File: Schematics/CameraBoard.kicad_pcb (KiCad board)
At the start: 2 copper layers, 62.3 x 68 mm, 61 parts, among them J1 Runcam Split 4 v2, J2 USB_C_Receptacle, SW1 SW_Push, SW2 SW_Push, U1 STM32F405RGTx, U2 TPS22917DBVR, U3 TPS22917DBVR, U4 SN65HVD230DR, U5 AMS1117-3.3, U6 TPS22917DBVR

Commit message: began routing
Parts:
- removed J1: Runcam Split 4 v2, Capacitor_SMD:C_0805_2012Metric_Pad1.18x1.45mm_HandSolder
- removed the REF** at (61.4, 55.5)
- added REF**: PinHeader_1x04_P2.00mm_Vertical, Connector_PinHeader_2.00mm:PinHeader_1x04_P2.00mm_Vertical, F.Cu at (64.0, 110.9)
- moved R1 18.1 mm to (105.1, 105.5), turned to 180 degrees
- moved R6 14.3 mm to (74.1, 51.5)
- moved C15 13.3 mm to (102.8, 103.5), turned to 0 degrees
- moved R2 10.8 mm to (99.6, 91.9), turned to 90 degrees
- moved C13 9.27 mm to (102.9, 101.4), turned to 0 degrees
- moved C12 9.03 mm to (102.7, 92.7)
- moved C14 5.46 mm to (102.8, 99.3), turned to 0 degrees
- moved R5 4.63 mm to (84.2, 56.0), turned to 0 degrees
- moved R7 3.92 mm to (80.9, 92.0)
- moved C24 2.99 mm to (77.2, 92.0), turned to 180 degrees
- moved U2 2.39 mm to (100.6, 96.0), turned to -90 degrees
- moved D1 1.72 mm to (79.8, 57.6), turned to 90 degrees
- moved U3 0.79 mm to (77.3, 95.2)
- moved C28 0.47 mm to (91.1, 92.5), turned to 180 degrees
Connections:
- D1 pad 1: /usb_type_c/D+ -> unconnected-(D1-Pad1)
- D1 pad 4: unconnected-(D1-Pad4) -> /usb_type_c/D+
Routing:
- net +3.3V: track 0.22 -> 135.6 mm
- net GND: track 0.00 -> 71.9 mm, vias 0 -> 2
- net +5V: track 0.00 -> 56.6 mm
- net /MCU/D+: track 0.00 -> 46.9 mm, vias 0 -> 6
- net (no net): track 0.00 -> 40.8 mm, vias 0 -> 5
- net /MCU/D-: track 0.00 -> 39.7 mm, vias 0 -> 2
- net /usb_type_c/D-: track 0.00 -> 14.4 mm
- net /Camera_right/<NO NET>: track 0.00 -> 13.8 mm
- net /Camera_center/<NO NET>: track 0.00 -> 12.3 mm
- net /Camera_left/<NO NET>: track 0.00 -> 11.8 mm
- net /usb_type_c/D+: track 0.00 -> 9.56 mm
- net /Camera_right/CAM_R_PWN_EN: track 0.00 -> 7.29 mm
- net Net-(J2-CC2): track 0.00 -> 7.08 mm
- net /Camera_right/CAM_UART_TX: track 0.00 -> 4.24 mm
- net /Camera_left/CAM_UART_TX: track 0.00 -> 3.93 mm
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
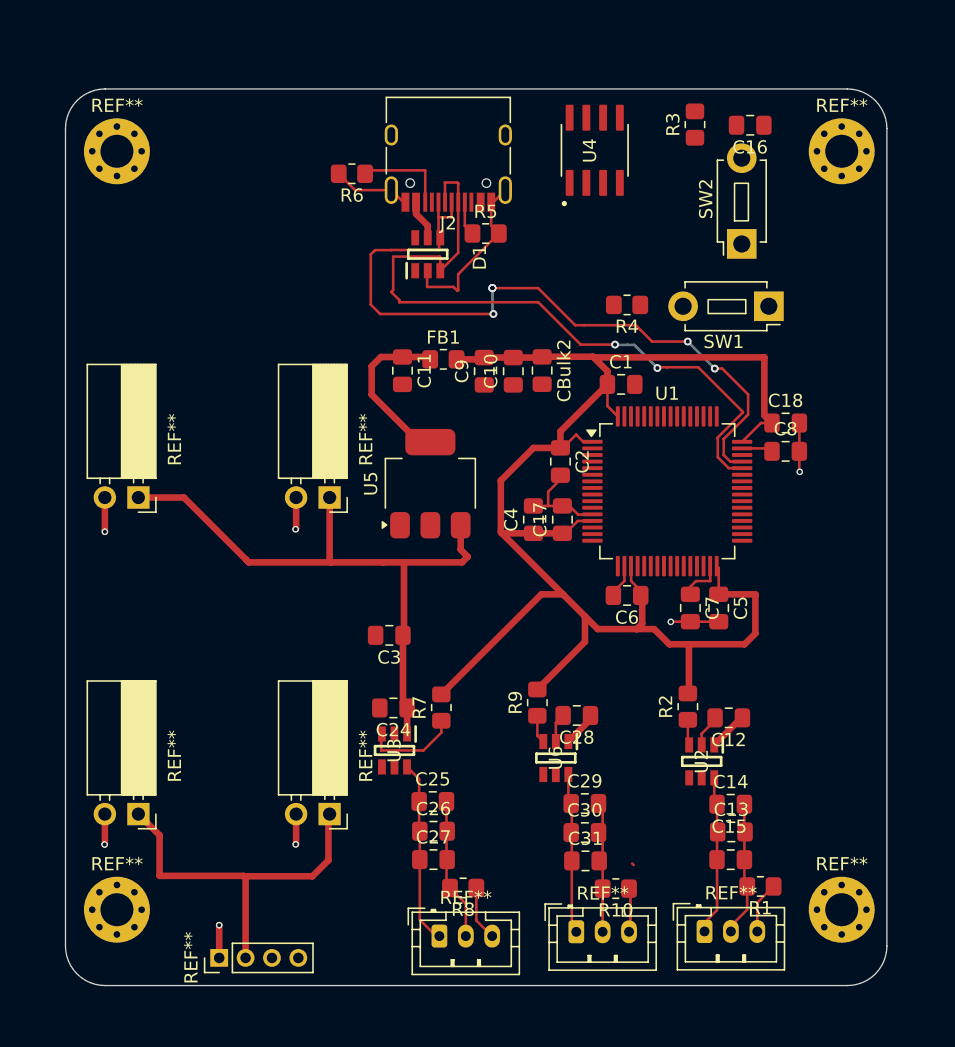
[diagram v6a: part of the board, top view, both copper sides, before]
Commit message: fixing routing redefining layout
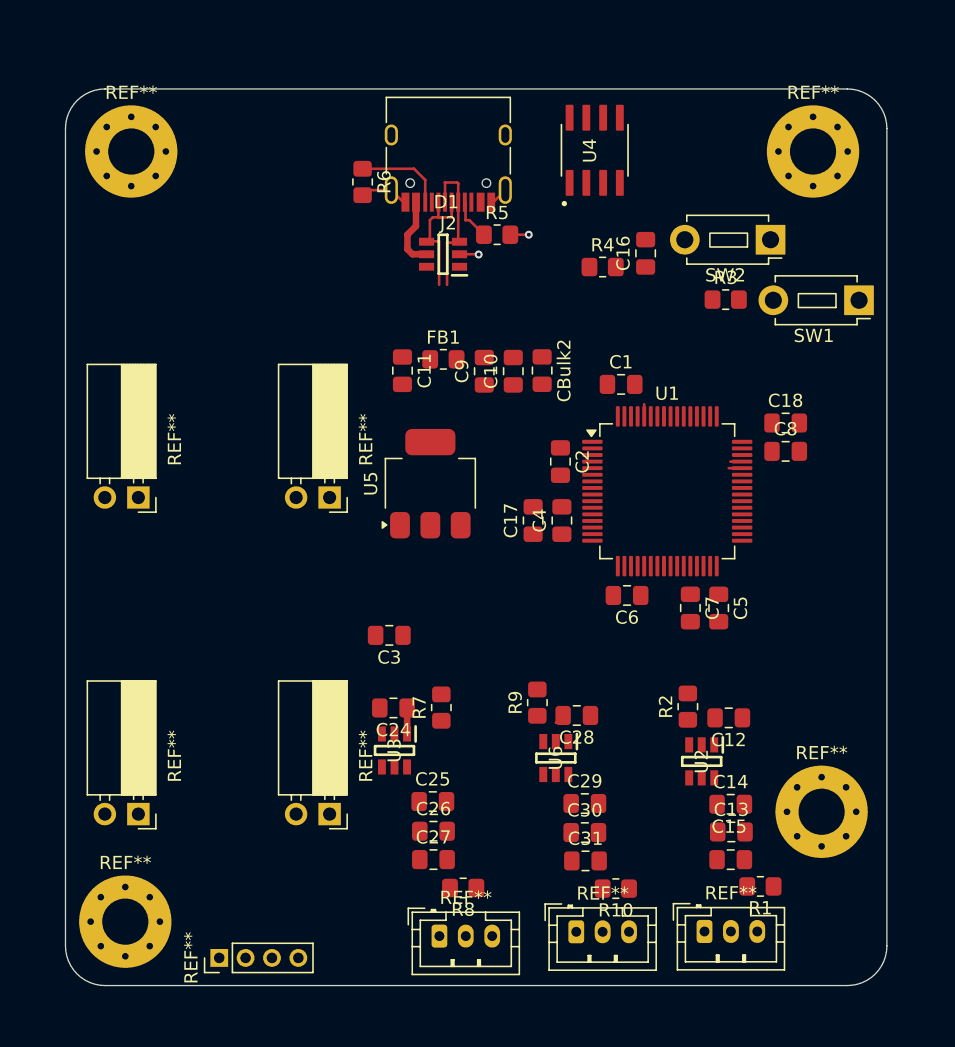
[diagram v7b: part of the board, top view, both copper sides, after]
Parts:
- removed the REF** at (56.3, 49.8)
- removed the REF** at (111.2, 107.3)
- removed the REF** at (111.2, 49.8)
- removed the REF** at (56.3, 107.3)
- added REF**: MountingHole_3.5mm_Pad_Via, MountingHole:MountingHole_3.5mm_Pad_Via, F.Cu at (56.9, 108.2)
- added REF**: MountingHole_3.5mm_Pad_Via, MountingHole:MountingHole_3.5mm_Pad_Via, F.Cu at (57.4, 49.8)
- added REF**: MountingHole_3.5mm_Pad_Via, MountingHole:MountingHole_3.5mm_Pad_Via, F.Cu at (109.7, 99.8)
- added REF**: MountingHole_3.5mm_Pad_Via, MountingHole:MountingHole_3.5mm_Pad_Via, F.Cu at (109.0, 49.8)
- moved R3 13.5 mm to (102.4, 61.0), turned to 0 degrees
- moved C16 12.5 mm to (96.4, 57.5), turned to 90 degrees
- moved SW1 6.86 mm to (112.5, 61.1)
- moved R4 3.42 mm to (93.1, 58.5), turned to 0 degrees
- moved C17 2.22 mm to (87.8, 77.8)
- moved SW2 2.20 mm to (105.8, 56.5), turned to 180 degrees
- moved C4 2.16 mm to (90.0, 77.8)
- moved D1 1.16 mm to (81.0, 57.6), turned to 180 degrees
- moved R6 1.02 mm to (74.9, 52.1), turned to -90 degrees
- moved R5 0.87 mm to (85.1, 56.1)
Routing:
- net +3.3V: track 135.6 -> 3.38 mm
- net GND: track 71.9 -> 11.3 mm
- net +5V: track 56.6 -> 8.35 mm
- net /MCU/D+: track 46.9 -> 0.89 mm, vias 6 -> 0
- net (no net): track 40.8 -> 0.42 mm, vias 5 -> 0
- net /MCU/D-: track 39.7 -> 1.02 mm, vias 2 -> 0
- net /Camera_right/<NO NET>: track 13.8 -> 0.07 mm
- net /Camera_center/<NO NET>: track 12.3 -> 0.68 mm
- net /Camera_left/<NO NET>: track 11.8 -> 0.30 mm
- net /Camera_right/CAM_R_PWN_EN: track 7.29 -> 0.08 mm
- net /Camera_right/CAM_UART_TX: track 4.24 -> 0.00 mm
- net /Camera_left/CAM_UART_TX: track 3.93 -> 0.00 mm
- net /Camera_center/CAM_UART_TX: track 3.54 -> 0.00 mm
- net Net-(U1-VCAP_1): track 3.40 -> 0.01 mm
- net /usb_type_c/D-: track 14.4 -> 11.4 mm
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
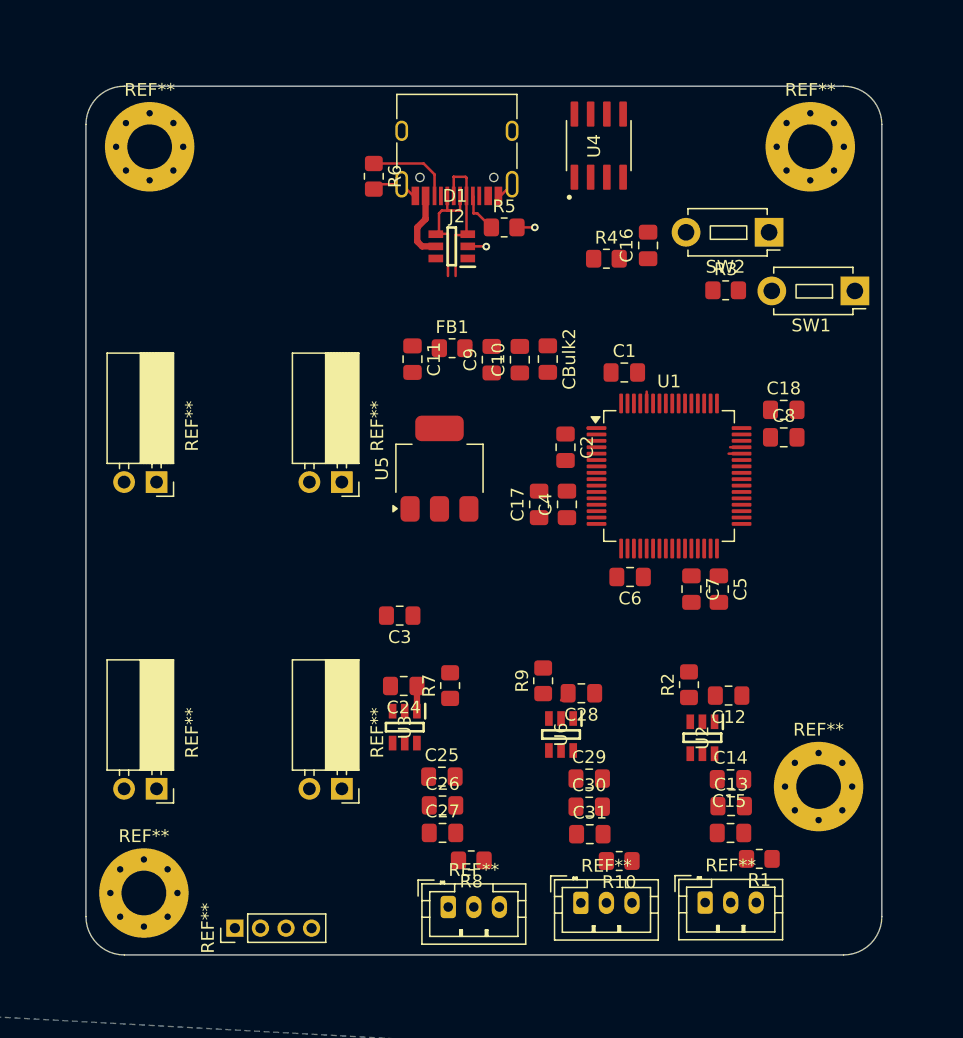
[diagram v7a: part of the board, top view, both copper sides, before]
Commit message: finalizing layout and saving space add all correct connectors and components
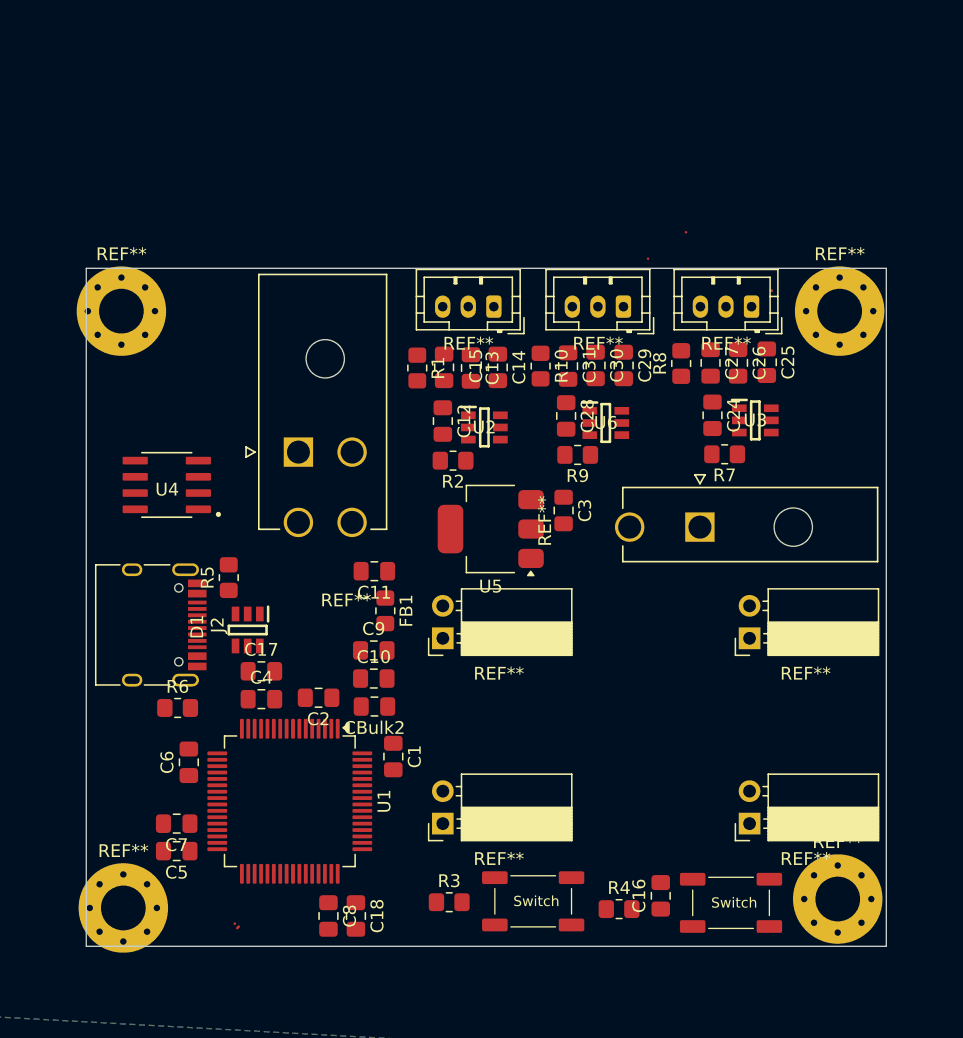
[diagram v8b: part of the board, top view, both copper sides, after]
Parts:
- removed the REF** at (64.0, 110.9)
- removed SW1, SW2: SW_Push, Button_Switch_THT:SW_PUSH_1P1T_6x3.5mm_H5.0_APEM_MJTP1250
- added REF**: MOLEX_26013114, myFootprints:MOLEX_26013114, F.Cu at (100.4, 79.5)
- added REF**: MOLEX_26013115, myFootprints:MOLEX_26013115, F.Cu at (69.0, 73.7)
- added Switch: SAMZO G4R0015010, Button_Switch_THT:SAMZO G4R0015010, F.Cu at (102.8, 109.0)
- added Switch: SAMZO G4R0015010, Button_Switch_THT:SAMZO G4R0015010, F.Cu at (87.4, 108.8)
- moved REF** 52.6 mm to (104.5, 62.3), turned to 180 degrees
- moved R3 52.5 mm to (80.8, 108.9)
- moved C18 51.9 mm to (73.5, 110.0), turned to -90 degrees
- moved C8 51.7 mm to (71.4, 110.0), turned to -90 degrees
- moved C16 50.9 mm to (97.3, 108.4)
- moved R4 50.9 mm to (94.1, 109.4)
- moved REF** 49.5 mm to (84.3, 62.3), turned to 180 degrees
- moved REF** 48.0 mm to (104.3, 88.2), turned to 180 degrees
- moved C5 47.1 mm to (59.5, 104.9), turned to 180 degrees
- moved R1 46.8 mm to (78.3, 67.1), turned to -90 degrees
- moved REF** 46.8 mm to (94.4, 62.3), turned to 180 degrees
- moved J2 44.8 mm to (57.0, 87.2), turned to -90 degrees
- moved R6 44.3 mm to (59.5, 93.7), turned to 0 degrees
- moved C7 44.3 mm to (59.5, 102.8), turned to 180 degrees
- moved U4 43.0 mm to (58.7, 76.2), turned to 180 degrees
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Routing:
- net /usb_type_c/D-: track 11.4 -> 0.00 mm
- net GND: track 11.3 -> 0.08 mm, vias 2 -> 0
- net /usb_type_c/D+: track 10.6 -> 0.00 mm
- net +5V: track 8.35 -> 0.00 mm
- net Net-(J2-CC2): track 7.15 -> 0.00 mm
- net Net-(J2-CC1): track 3.24 -> 0.00 mm
- net +3.3V: track 3.38 -> 0.76 mm
- net /MCU/D-: track 1.02 -> 0.00 mm
- net /MCU/BOOT0: track 1.00 -> 0.00 mm
- net /MCU/D+: track 0.89 -> 0.00 mm
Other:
- board size 62.3 x 68 mm -> 62.6 x 53 mm
